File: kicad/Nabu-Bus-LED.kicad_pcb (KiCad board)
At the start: 2 copper layers, 144.8 x 106.3 mm, 69 parts, among them J1 Nabu_Bus_IN, J2 Nabu_Bus_IN_TestPoints, J3 Nabu_Bus_OUT_TestPoints, J4 Nabu_Bus_OUT, J6 Banana_-12V, J7 Banana_+12V, J8 Banana_+5V, J9 Banana_Ground

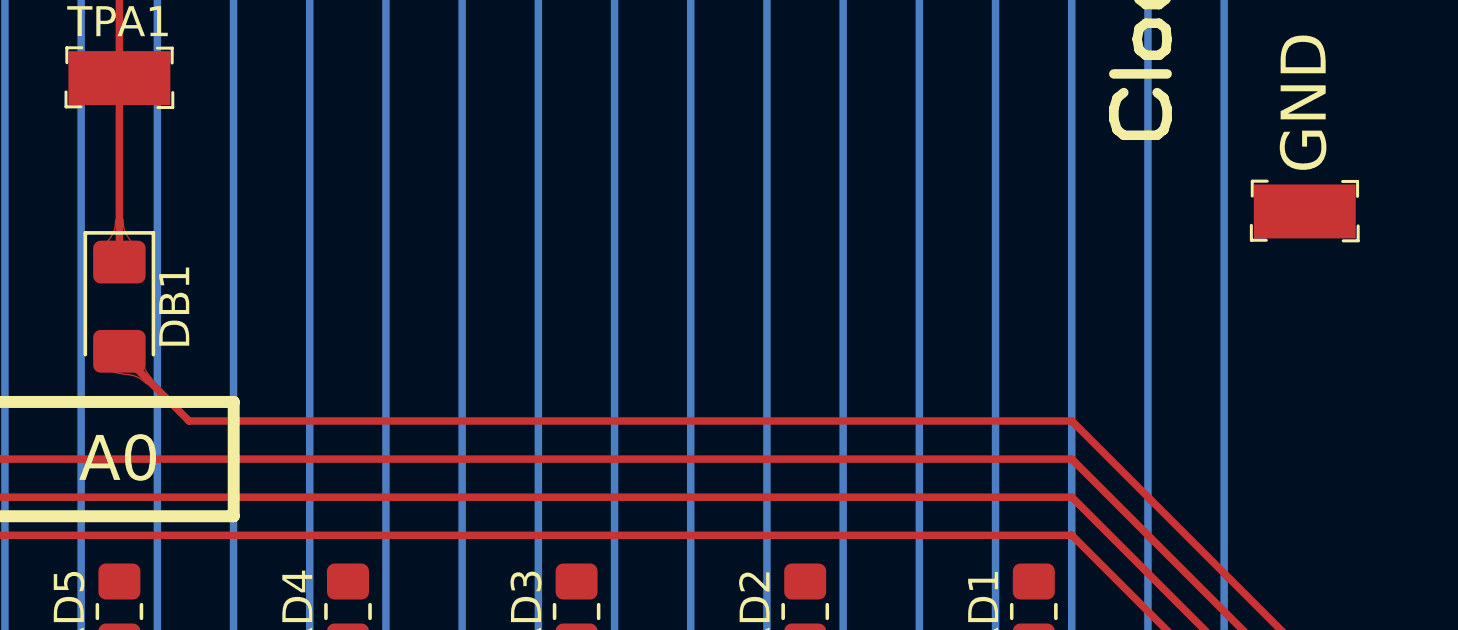
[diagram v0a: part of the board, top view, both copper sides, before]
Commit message: Added "Remixed by Symax" label.
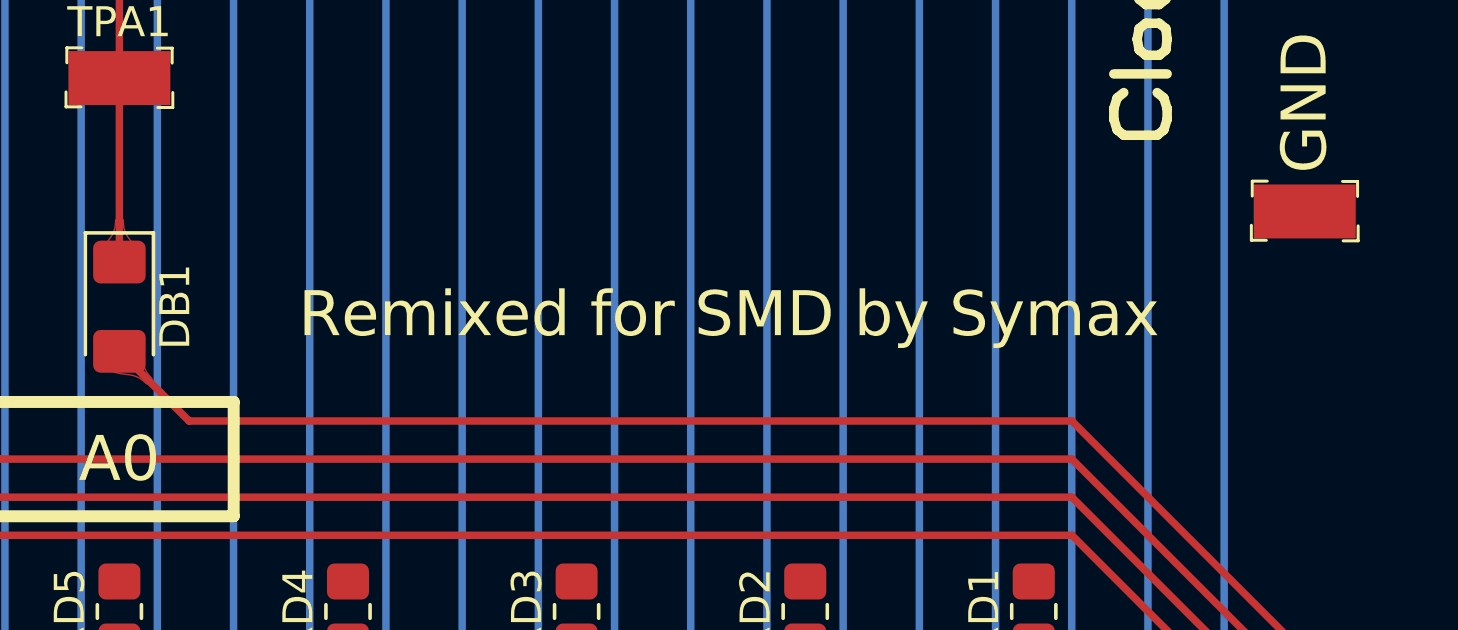
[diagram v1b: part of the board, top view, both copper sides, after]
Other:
- board text added: "Remixed for SMD by Symax"
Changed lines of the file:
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@@
+    (effects (font (size 1.5 1.5) (thickness 0.3)))
+  )
+  (gr_text "Remixed for SMD by Symax" (at 84.455 101.219) (layer "F.SilkS")
     (effects (font (size 1.5 1.5) (thickness 0.3)))
   )
